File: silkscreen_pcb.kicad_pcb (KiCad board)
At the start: 2 copper layers, 60 x 111.3 mm, 177 parts, among them J1 USB_C_Receptacle, J2 FH34SRJ-24S-0.5SH_50_, J3 FH34SRJ-6S-0.5SH_50_, J4 FH34SRJ-6S-0.5SH_50_, J5 Conn_01x02, J6 PPPC062LJBN-RC, J7 Micro_SD_Card, Q1 FS8205A, Q3 AO3419, Q4 BSS138, Q5 BSS138, Q6 BSS138, Q7 AO3419, Q8 AO3419, SW1 SW_Push, SW10 SW_Push, SW11 SW_Push, SW2 SW_Push, SW3 SW_Push, SW4 SW_Push, SW5 SW_Push, SW6 SW_Push, SW7 SW_Push, SW8 SW_Push, SW9 SW_Push, U1 TPD4E1U06DBVR, U10 TPS923610DRLR, U11 TP4056-42-ESOP8, U12 74LVC1G04, U13 DS3231MZ, U2 TPS2116DRL, U3 TLV75533PDBV, U4 ESP32-S3-WROOM-1, U5 DW01A, U6 TPD4E1U06DBVR, U7 TPD4E1U06DBVR, U8 TPD4E1U06DBVR, U9 TPD4E1U06DBVR

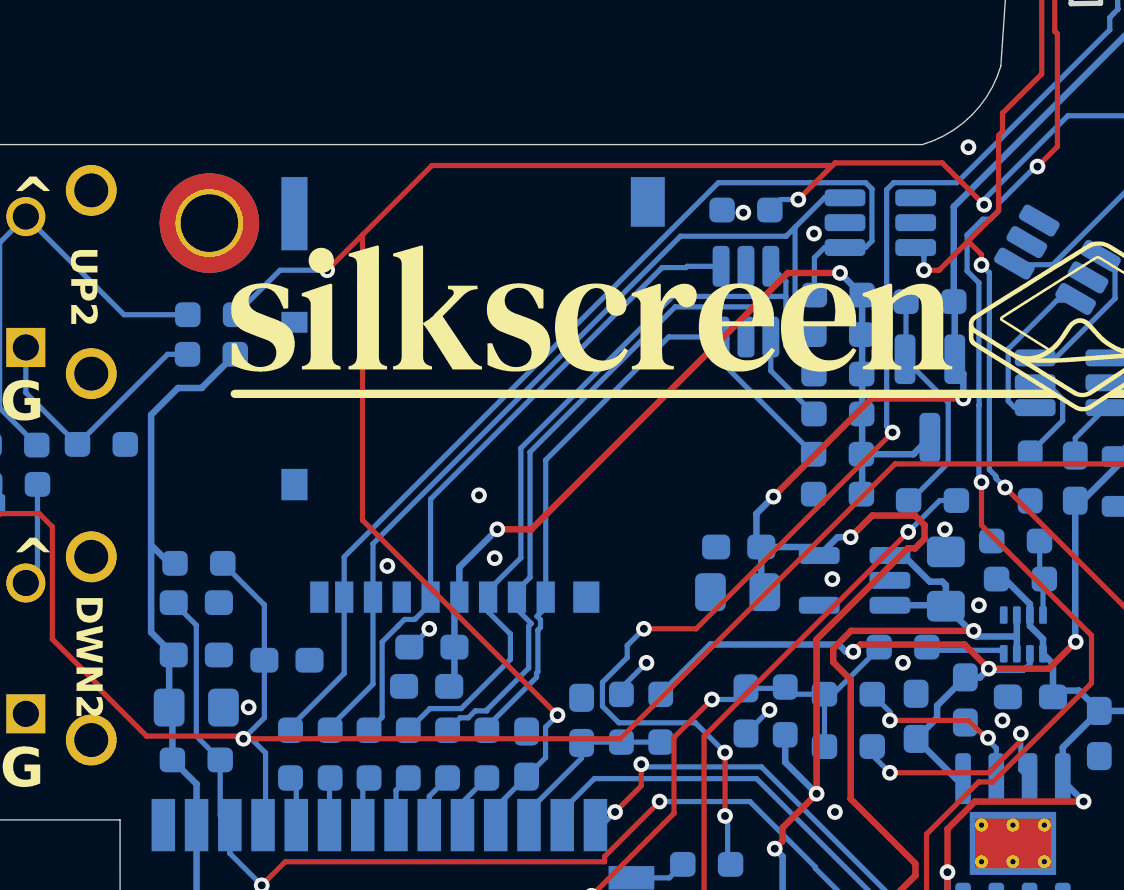
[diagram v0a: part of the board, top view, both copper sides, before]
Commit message: microSD: dual-source push-push footprint (TF PUSH / MEM2075) + doc/BOM sync
- Add project-local microSD_dualsource footprint accepting SHOU HAN TF PUSH
  (LCSC C393941, JLC builds) or GCT MEM2075-00-140-01-A (DigiKey). Built from
  the exact SHOU HAN DXF + GCT .kicad_mod, with FastEDA WRL 3D model. Pinout
  identical to Hirose DM3AT (1-8 signals, 9=shield/GND); replaces the push-pull
  DM3AT on J7. fp-lib-table registers the new library.
- BOM/docs sync to settled parts: J7 push-push (MEM2075 DigiKey / TF PUSH JLC);
  L2 -> VLS252010HBU-4R7M (C413592); U4 -> N16R8; SW1-11 tactiles note TS365ZJ
  (C557598); CR1-3 note SD05C alt; SW6 -> DNP.
- DESIGN_REVIEW: add microSD connector-swap note; fix stale 6.9 nit (SD VDD is
  gated by Q7, not hard-wired; C37 is 1uF).
- THIRD_PARTY: attribute microSD footprint sources + FastEDA WRL model.
- Recolor FH34SRJ 24-pin 3D STEP (placeholder magenta/cyan -> dark plastic +
  silver shell).
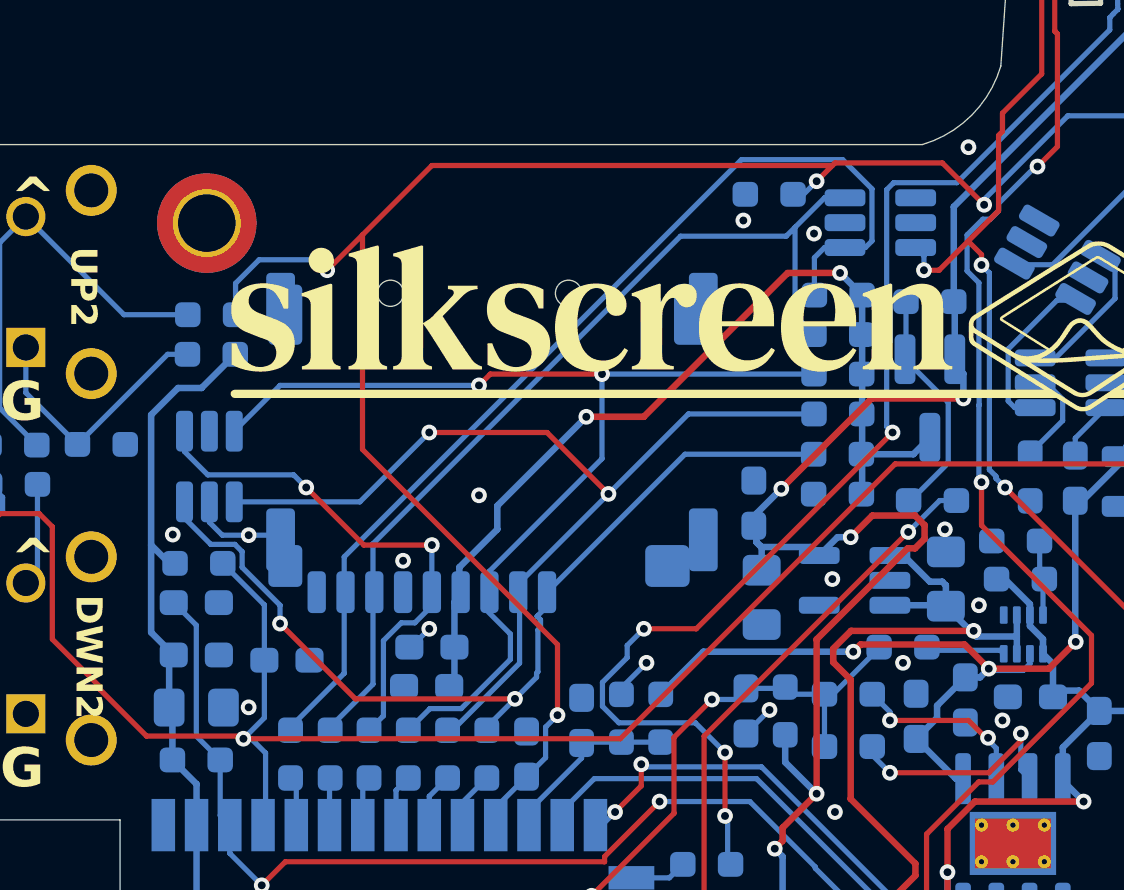
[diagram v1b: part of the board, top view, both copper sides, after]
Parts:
- J7: footprint Connector_Card:microSD_HC_Hirose_DM3AT-SF-PEJM5 -> microSD_dualsource:microSD_PushPush_TFPUSH-MEM2075
- moved U1 21.4 mm to (54.0, 79.8)
- moved J7 7.60 mm to (63.0, 84.6)
- moved C21 1.77 mm to (74.8, 81.2), turned to 90 degrees
- moved R76 1.07 mm to (75.4, 69.4)
- moved C6 0.94 mm to (75.1, 84.8), turned to -90 degrees
- moved H2 0.10 mm to (53.9, 70.5)
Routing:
- net SD_DAT2: track 25.6 -> 35.0 mm, vias 0 -> 2
- net SD_CMD: track 31.4 -> 40.2 mm, vias 0 -> 2
- net SD_DAT3: track 28.8 -> 37.2 mm, vias 0 -> 2
- net SD_CLK: track 24.8 -> 20.1 mm, vias 0 -> 2
- net GND: track 16.4 -> 20.3 mm, vias 46 -> 47
- net SD_DAT1: track 39.1 -> 39.9 mm
- net 3V3: track 314.1 -> 313.5 mm
- net SD_VDD: track 35.6 -> 36.1 mm

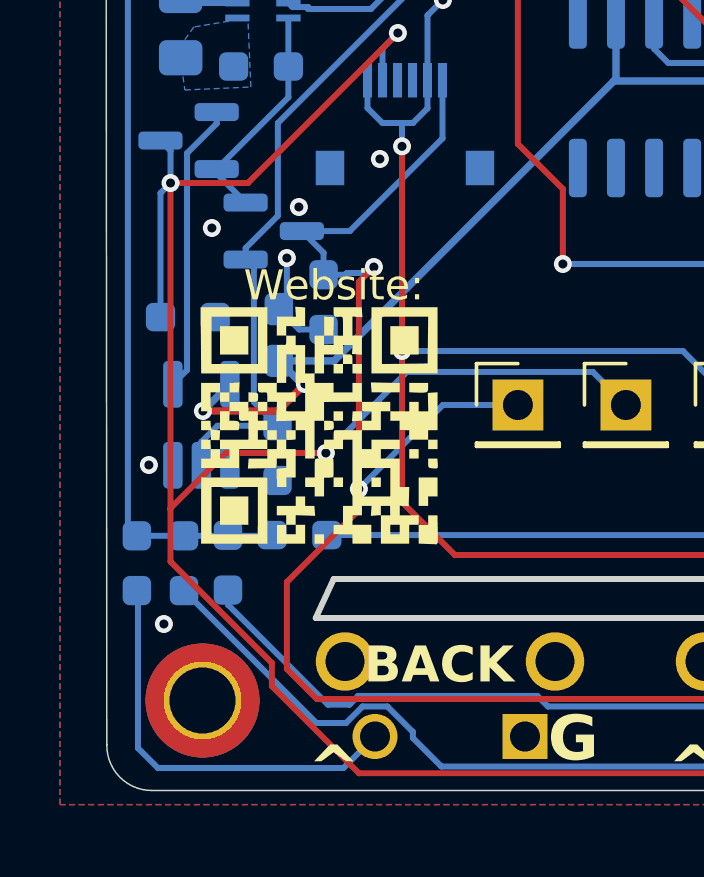
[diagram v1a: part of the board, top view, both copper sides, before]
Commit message: Prototype-run release: button re-center, schematic cleanup, doc refresh, as-ordered BOM
Board / schematic:
- Re-center bottom button row (SW2/SW3/SW8/SW9) on the board (was 2.5 mm right
  of center; now 11.5 mm margin each side, 12/13/12 spacing kept).
- Fix stale AP3031-era net name and the LED_MONIT/ADC annotation.

Docs:
- Regenerate full schematic capture (full-capture.png) and per-block images;
  add PCB layout plot (silkscreen_pcb_layout.pdf).
- Remove superseded assets (board-3d-top.png, 00-full-sheet.png,
  18-color-select.png, silkscreen_pcb.pdf) and repoint all README/HARDWARE/
  DESIGN_REVIEW links to the current plots.
- Document SW6 (BOOT/IO0) as DNP + USB-Serial-JTAG download path (HARDWARE 9.3,
  DESIGN_REVIEW); fix the stale 6.9 microSD-VDD nit.

Fabrication:
- Add the as-ordered JLC BOM (production/bom_JLC_upload.csv): clean 4-column
  format with the settled LCSC parts (TS365ZJ tactiles, TF PUSH microSD, SD05C,
  cheaper 22 uF, L2 VLS252010HBU-4R7M) and all DNP components listed for
  completeness (U13 DS3231MZ+, SW6, R43/R45/R58/R66/R72/R74).

This is the design state for the first JLCPCB prototype run.
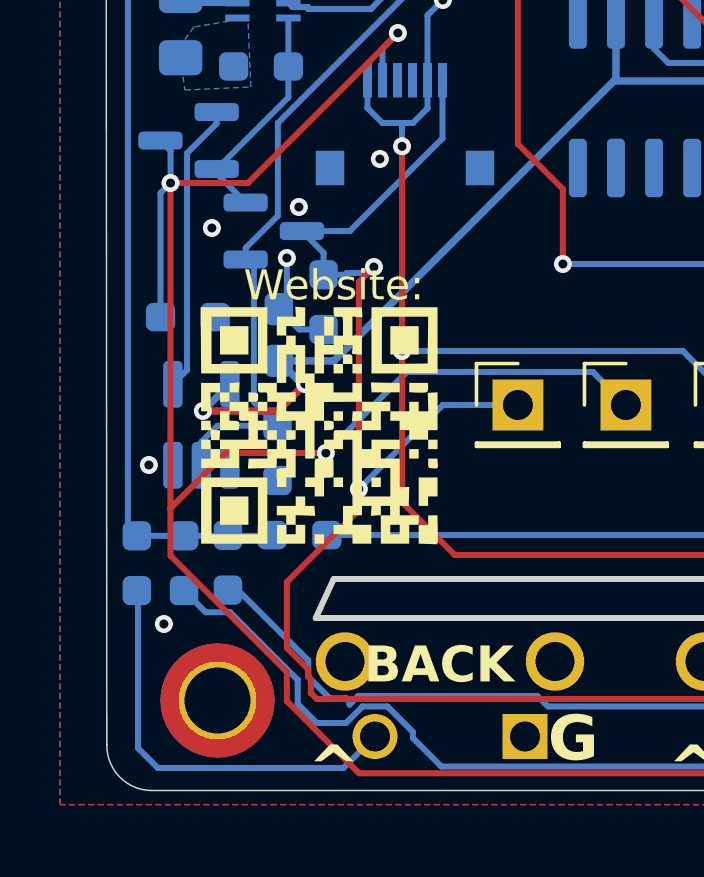
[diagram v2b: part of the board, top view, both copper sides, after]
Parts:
- moved H3 0.50 mm to (48.0, 145.2)
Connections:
- net 3031_SW renamed TPS_SW_NODE
